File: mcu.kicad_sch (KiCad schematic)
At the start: 25 parts, among them J1 Conn_ARM_JTAG_SWD_20, SW1 SW_SPST, U10 WE-TVS-824015043, U6 STM32F469VETx

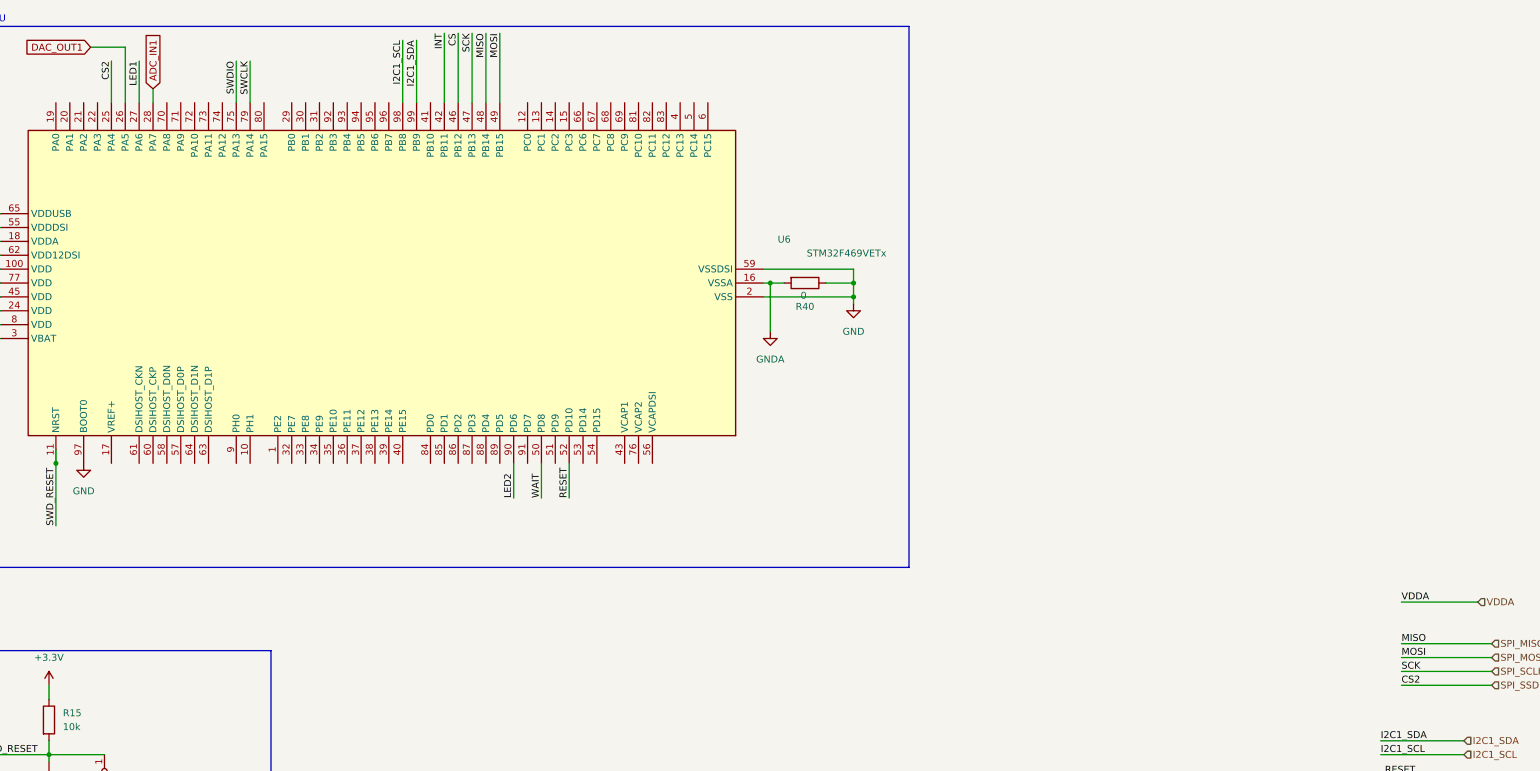
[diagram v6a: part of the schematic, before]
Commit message: wired SD card
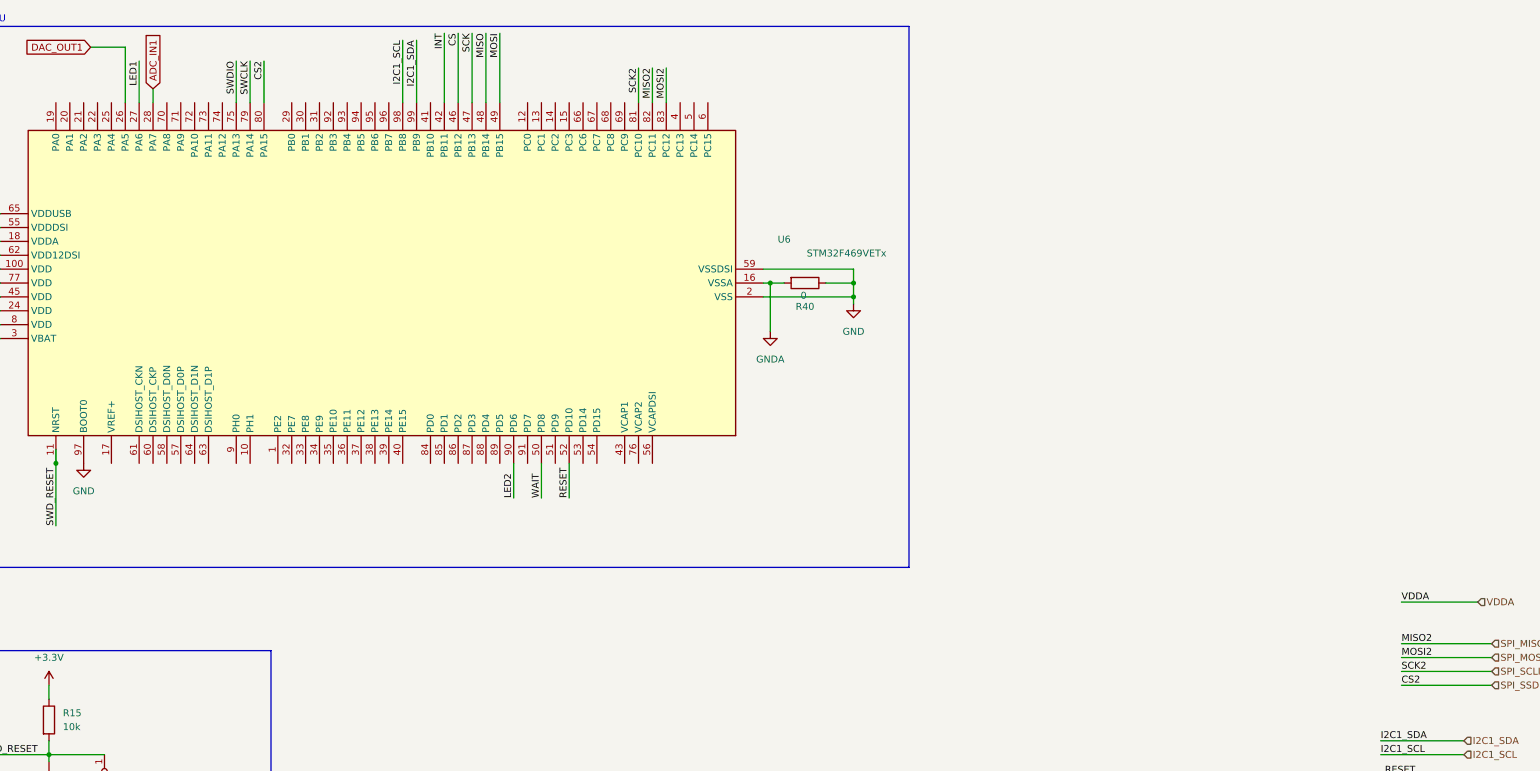
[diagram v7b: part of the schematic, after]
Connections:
- net SPI_SSD: now also U6.80 (PA15); no longer U6.25 (PA4)
- net SPI_SCLK: now reaches U6.81 (PC10)
- net SPI_MISO: now reaches U6.82 (PC11)
- net SPI_MOSI: now reaches U6.83 (PC12)
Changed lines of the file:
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@@
+	(wire
+		(pts
+			(xy 90.17 36.83) (xy 90.17 44.45)
+		)
+		(stroke
+			(width 0)
+			(type default)
+		)
+	)
 	(wire
 		(pts
@@
 	(wire
 		(pts
+			(xy 163.83 38.1) (xy 163.83 44.45)
+		)
+		(stroke
+			(width 0)
+			(type default)
+		)
+	)
+	(wire
+		(pts
 			(xy 181.61 80.01) (xy 198.12 80.01)
 		)
@@
 	(wire
 		(pts
-			(xy 62.23 36.83) (xy 62.23 44.45)
+			(xy 161.29 38.1) (xy 161.29 44.45)
 		)
 		(stroke
@@
 	(wire
 		(pts
+			(xy 158.75 38.1) (xy 158.75 44.45)
+		)
+		(stroke
+			(width 0)
+			(type default)
+		)
+	)
+	(wire
+		(pts
 			(xy 147.32 224.79) (xy 154.94 224.79)
 		)
@@
 		)
 	)
-	(label "MISO"
+	(label "MISO2"
 		(at 298.45 143.51 0)
 		(effects
@@
 		)
 	)
-	(label "SCK"
+	(label "SCK2"
 		(at 298.45 148.59 0)
 		(effects
@@
 		)
 	)
-	(label "CS2"
-		(at 62.23 36.83 270)
-		(effects
-			(font
-				(size 1.27 1.27)
-			)
-			(justify right bottom)
-		)
-	)
 	(label "SWDIO"
 		(at 104.14 242.57 180)
@@
 		)
 	)
+	(label "SCK2"
+		(at 158.75 38.1 270)
+		(effects
+			(font
+				(size 1.27 1.27)
+			)
+			(justify right bottom)
+		)
+	)
 	(label "RESET"
 		(at 146.05 116.84 90)
@@
 		)
 	)
+	(label "MISO2"
+		(at 161.29 38.1 270)
+		(effects
+			(font
+				(size 1.27 1.27)
+			)
+			(justify right bottom)
+		)
+	)
 	(label "INT"
 		(at 300.99 182.88 180)
@@
 		)
 	)
+	(label "CS2"
+		(at 90.17 36.83 270)
+		(effects
+			(font
+				(size 1.27 1.27)
+			)
+			(justify right bottom)
+		)
+	)
 	(label "LED2"
 		(at 340.36 207.01 270)
@@
 		)
 	)
-	(label "MOSI"
+	(label "MOSI2"
 		(at 298.45 146.05 0)
 		(effects
@@
 		(effects
 			(font
+				(size 1.27 1.27)
+			)
+			(justify right bottom)
+		)
+	)
+	(label "MOSI2"
+		(at 163.83 38.1 270)
+		(effects
+			(font

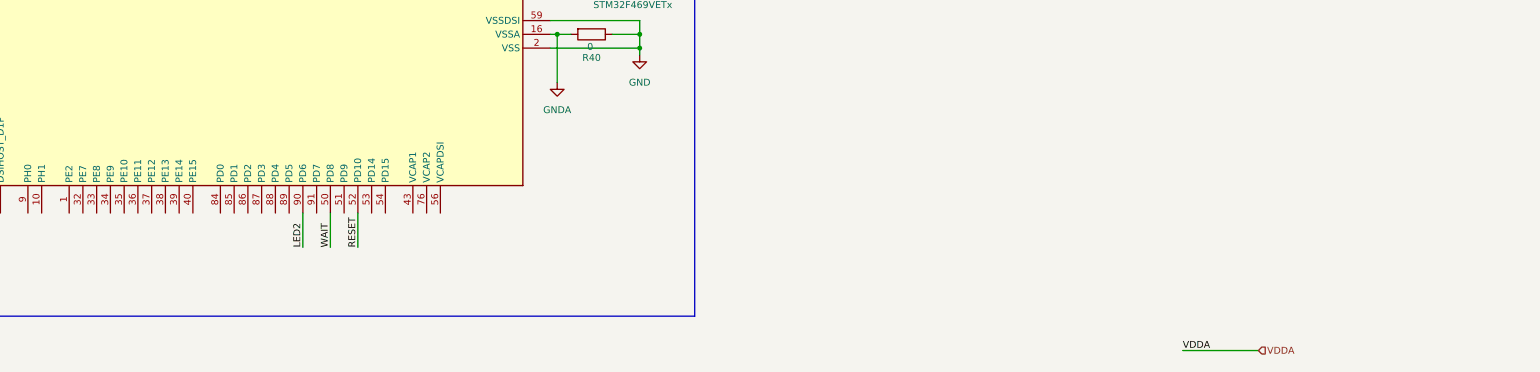
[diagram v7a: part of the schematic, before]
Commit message: added redundent spi
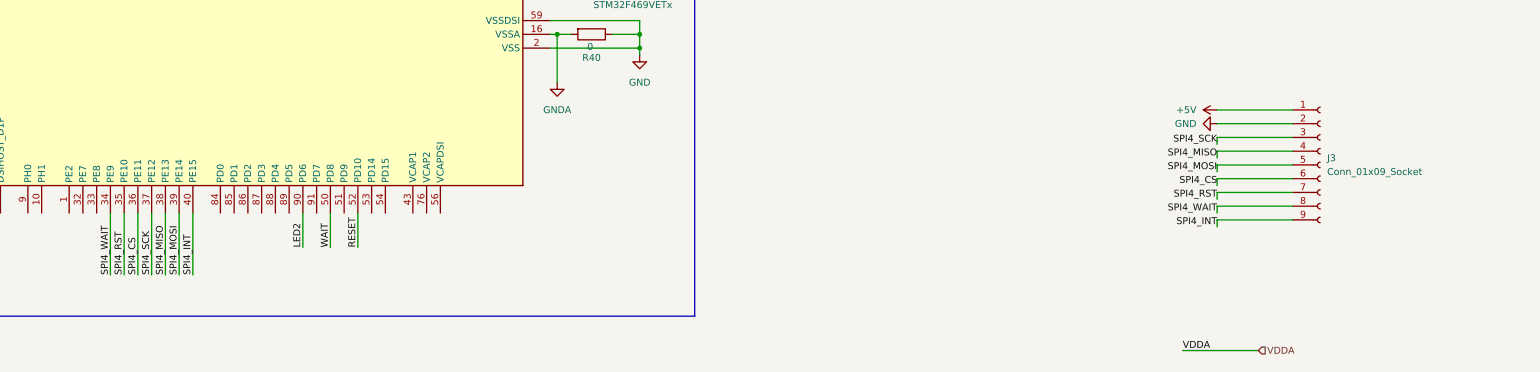
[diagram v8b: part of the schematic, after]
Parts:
- added J3: Conn_01x09_Socket, Connector_PinHeader_2.00mm:PinHeader_1x09_P2.00mm_Vertical, symbol Connector:Conn_01x09_Socket
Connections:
- net GND: now also J3.2 (Pin_2)
- net SPI4_WAIT: now reaches U6.34 (PE9)
- net SPI4_WAIT: now also J3.8 (Pin_8)
- net SPI4_RST: now reaches U6.35 (PE10)
- net SPI4_RST: now also J3.7 (Pin_7)
- net SPI4_CS: now reaches U6.36 (PE11)
- net SPI4_CS: now also J3.6 (Pin_6)
- net SPI4_SCK: now reaches U6.37 (PE12)
- net SPI4_SCK: now also J3.3 (Pin_3)
- net SPI4_MISO: now reaches U6.38 (PE13)
- net SPI4_MISO: now also J3.4 (Pin_4)
- net SPI4_MOSI: now reaches U6.39 (PE14)
- net SPI4_MOSI: now also J3.5 (Pin_5)
- net SPI4_INT: now reaches U6.40 (PE15)
- net SPI4_INT: now also J3.9 (Pin_9)
- new net +5V: J3.1 (Pin_1)
